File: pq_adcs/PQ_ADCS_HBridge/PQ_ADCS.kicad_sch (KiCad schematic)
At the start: 50 parts, among them J1 CES-110-02-L-S, J12 CES-102-02-L-S, J2 CES-110-02-L-S, J3 CES-110-02-L-S, J4 CES-110-02-L-S, J5 53261-1471, J6 53261-1471, J7 53261-1471, J8 53261-1471, U1 LPV542, U2 LPV542, U3 LPV542, U4 IIM-42652, U5 DRV8214RTER, U6 TMUX1108RSVR, U7 MMC5983MA, U8 DRV8214RTER, U9 DRV8214RTER

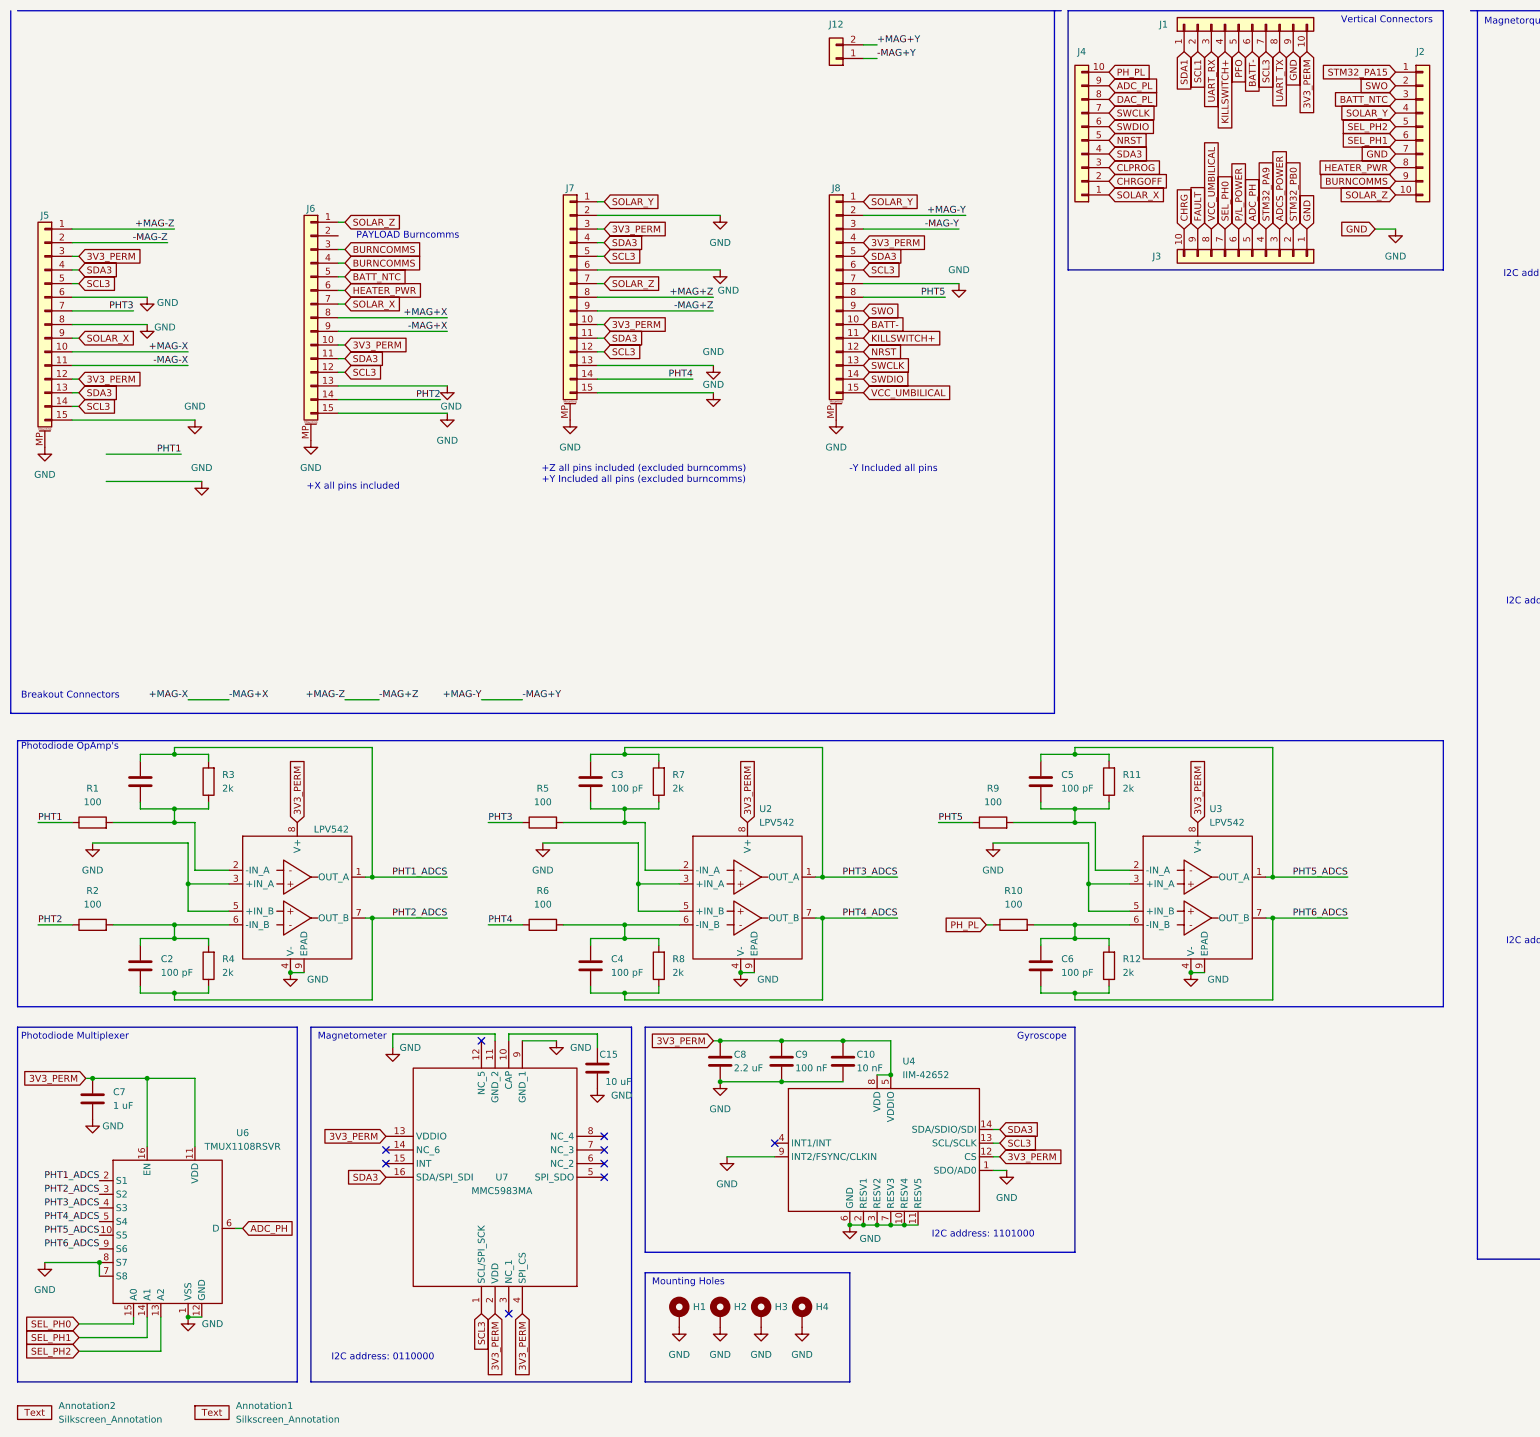
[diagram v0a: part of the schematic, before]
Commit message: ADCS_HBRIDGE backup restore
Restored version with H bridge and no connectors modification
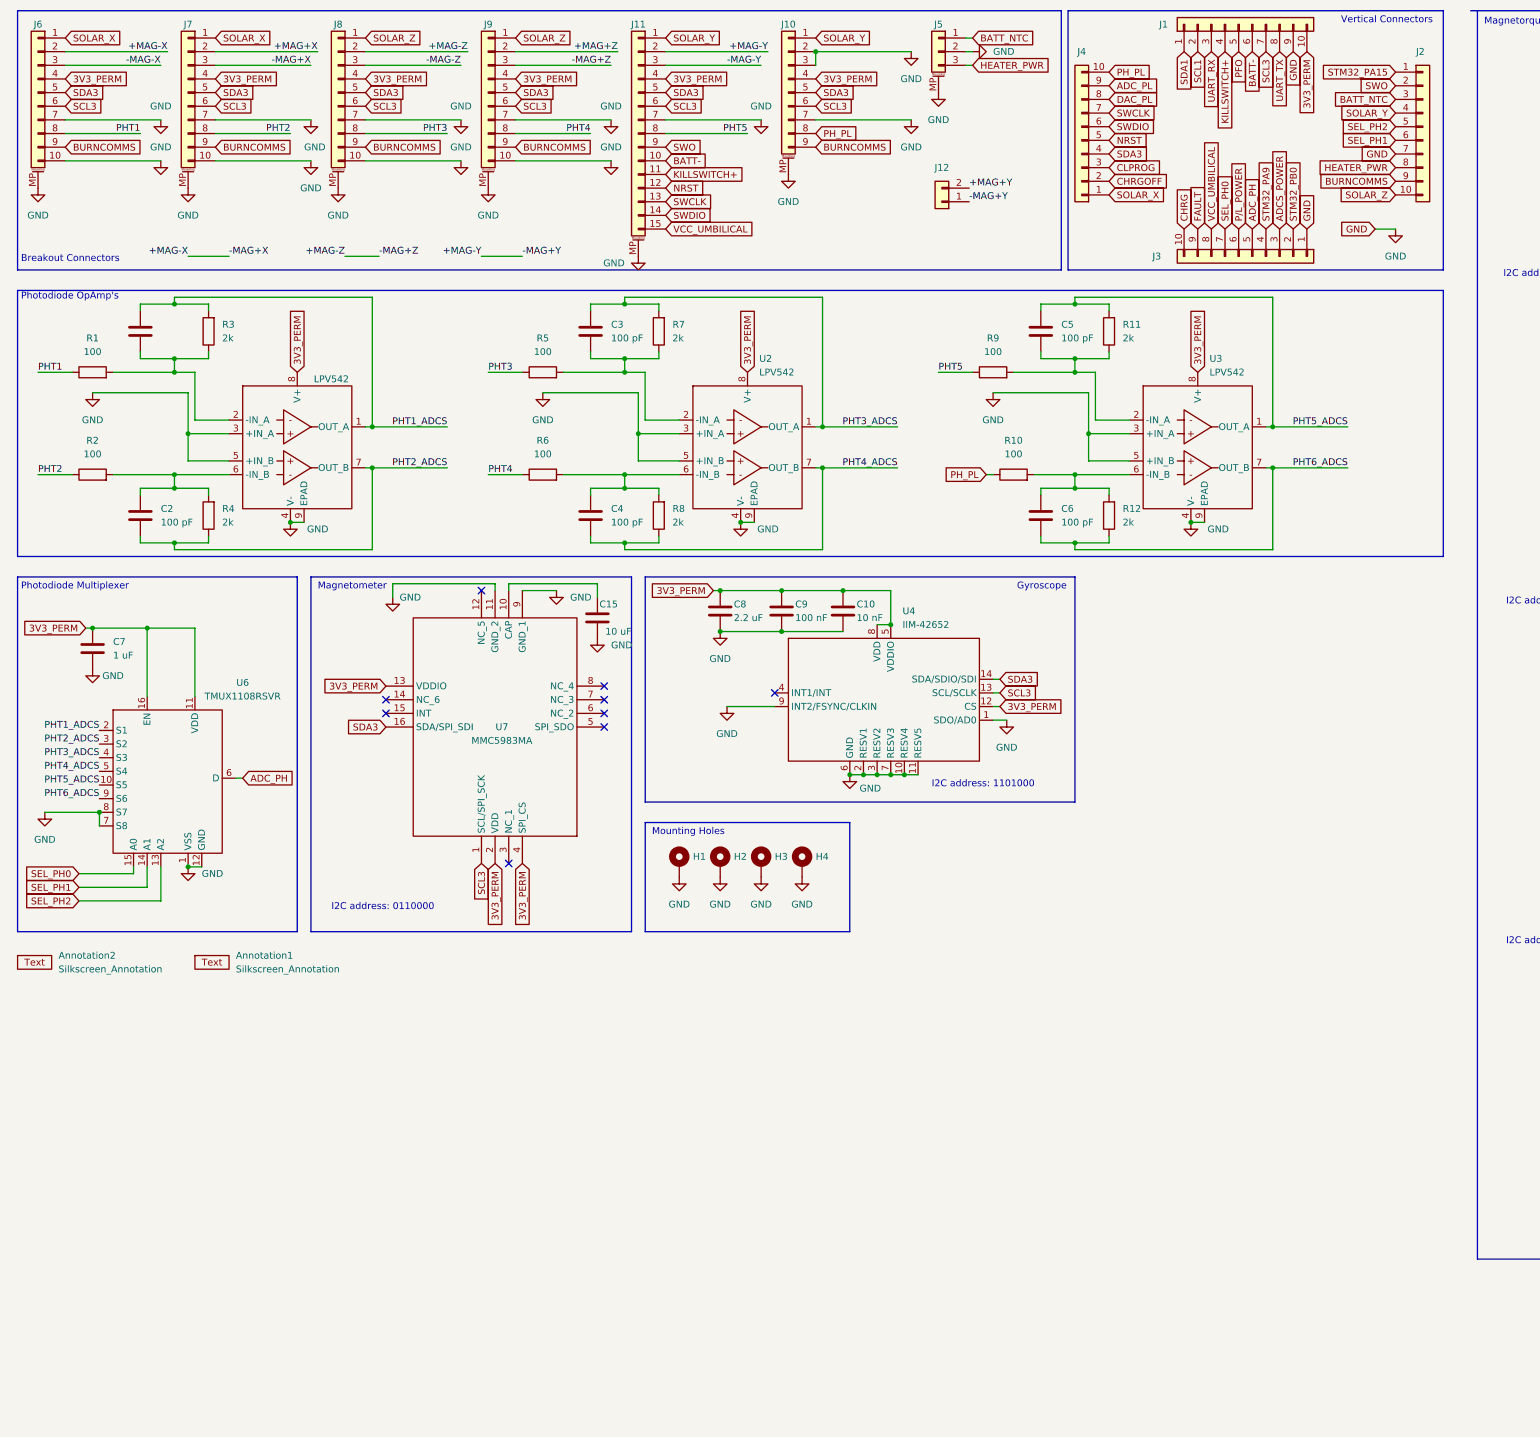
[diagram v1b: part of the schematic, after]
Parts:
- removed J5, J6, J7, J8: 53261-1471, Connector_Molex:Molex_PicoBlade_53261-1571_1x15-1MP_P1.25mm_Horizontal, symbol Connector_Generic_MountingPin:Conn_01x15_MountingPin
- added J10: Pico-Clasp_01x09, connector-nsl:Picoclasp09, symbol connector-nsl:Picoclasp09
- added J11: Pico-Clasp_01x15, connector-nsl:Picoclasp15, symbol connector-nsl:Picoclasp15
- added J5: Pico-Clasp_01x03, connector-nsl:Picoclasp03, symbol connector-nsl:Picoclasp03
- added J6, J7, J8, J9: Pico-Clasp_01x10, connector-nsl:Picoclasp10, symbol connector-nsl:Picoclasp10
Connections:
- net +MAG+X: now also J7.2
- net +MAG+Z: now also J9.2
- net +MAG-X: now also J6.2, J7.3
- net +MAG-Y: now also J11.2
- net +MAG-Z: now also J8.2, J9.3
- net -MAG-X: now also J6.3
- net -MAG-Y: now also J11.3
- net -MAG-Z: now also J8.3
- net 3V3_PERM: now also J10.4, J11.4, J6.4, J7.4, J8.4, J9.4
- net BATT-: now also J11.10
- net BATT_NTC: now also J5.1
- net BURNCOMMS: now also J10.9, J6.9, J7.9, J8.9, J9.9
- net GND: now also J10.2, J10.3, J10.7, J10.MP, J11.7, J11.MP, J5.2, J5.MP, J6.10, J6.7, J6.MP, J7.10, J7.7, J7.MP, J8.10, J8.7, J8.MP, J9.10, J9.7, J9.MP
- net HEATER_PWR: now also J5.3
- net KILLSWITCH+: now also J11.11
- net NRST: now also J11.12
- net PHT1: now also J6.8
- net PHT2: now also J7.8
- net PHT3: now also J8.8
- net PHT4: now also J9.8
- net PHT5: now also J11.8
- net PH_PL: now also J10.8
- net SCL3: now also J10.6, J11.6, J6.6, J7.6, J8.6, J9.6
- net SDA3: now also J10.5, J11.5, J6.5, J7.5, J8.5, J9.5
- net SOLAR_X: now also J6.1, J7.1
- net SOLAR_Y: now also J10.1, J11.1
- net SOLAR_Z: now also J8.1, J9.1
- net SWCLK: now also J11.13
- net SWDIO: now also J11.14
- net SWO: now also J11.9
- net VCC_UMBILICAL: now also J11.15
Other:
- note removed: "+X all pins included"
- note removed: "+Z all pins included (excluded burncomms) +Y Included all pins (excluded burncomms)"
- note removed: "-Y Included all pins"
- note removed: "PAYLOAD Burncomms"
- moved on the sheet: Annotation1, Annotation2, C10, C15, C2, C3, C4, C5, C6, C7, C8, C9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

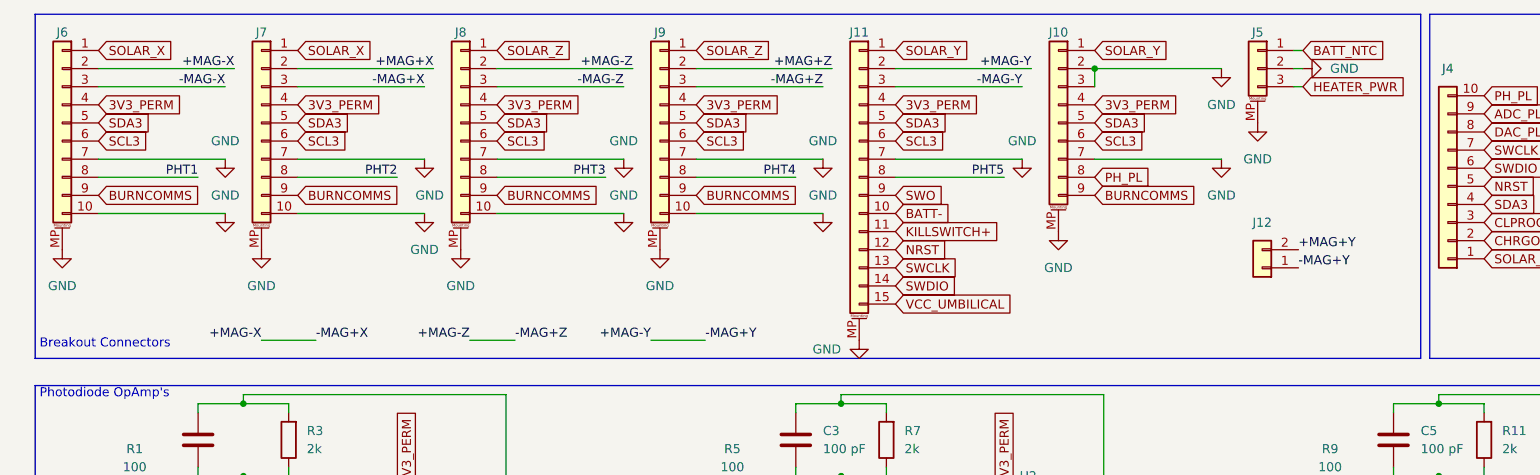
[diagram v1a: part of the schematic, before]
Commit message: MOdifying connectors ADCS H - Bridge
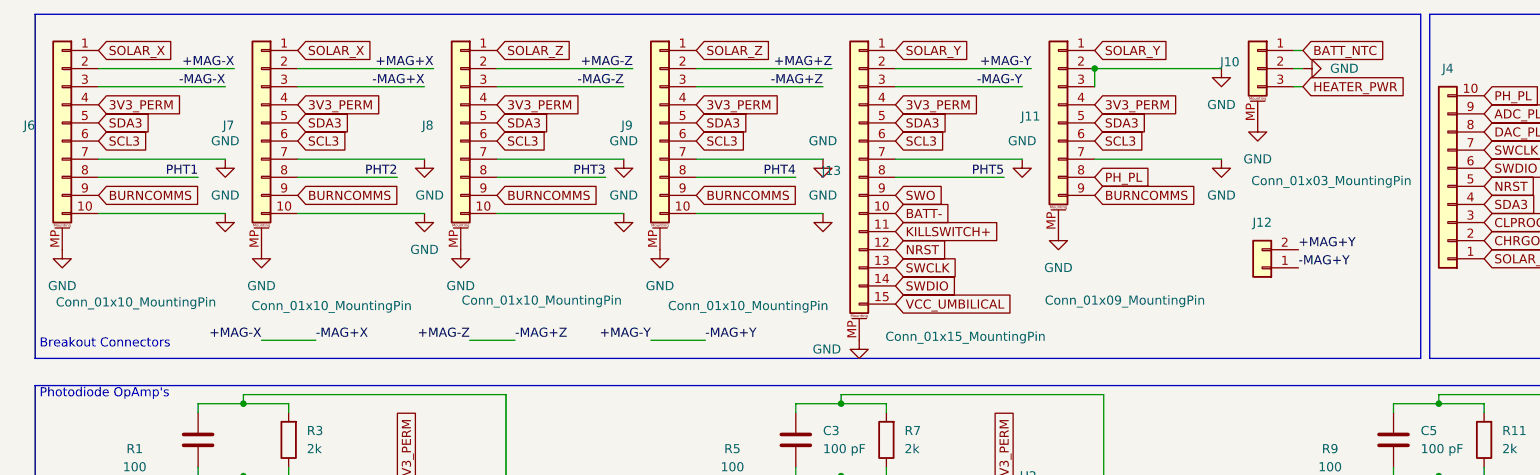
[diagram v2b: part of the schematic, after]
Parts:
- removed J10: Pico-Clasp_01x09, connector-nsl:Picoclasp09, symbol connector-nsl:Picoclasp09
- removed J11: Pico-Clasp_01x15, connector-nsl:Picoclasp15, symbol connector-nsl:Picoclasp15
- removed J5: Pico-Clasp_01x03, connector-nsl:Picoclasp03, symbol connector-nsl:Picoclasp03
- removed J6, J7, J8, J9: Pico-Clasp_01x10, connector-nsl:Picoclasp10, symbol connector-nsl:Picoclasp10
- added J10: Conn_01x03_MountingPin, Connector_Molex:Molex_PicoBlade_53261-0371_1x03-1MP_P1.25mm_Horizontal, symbol Connector_Generic_MountingPin:Conn_01x03_MountingPin
- added J11: Conn_01x09_MountingPin, Connector_Molex:Molex_PicoBlade_53261-0971_1x09-1MP_P1.25mm_Horizontal, symbol Connector_Generic_MountingPin:Conn_01x09_MountingPin
- added J13: Conn_01x15_MountingPin, Connector_Molex:Molex_PicoBlade_53261-1571_1x15-1MP_P1.25mm_Horizontal, symbol Connector_Generic_MountingPin:Conn_01x15_MountingPin
- added J6, J7, J8, J9: Conn_01x10_MountingPin, Connector_Molex:Molex_PicoBlade_53261-1071_1x10-1MP_P1.25mm_Horizontal, symbol Connector_Generic_MountingPin:Conn_01x10_MountingPin
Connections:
- net +MAG+X: now also J7.2 (Pin_2)
- net +MAG+Z: now also J9.2 (Pin_2)
- net +MAG-X: now also J6.2 (Pin_2), J7.3 (Pin_3)
- net +MAG-Y: now also J13.2 (Pin_2)
- net +MAG-Z: now also J8.2 (Pin_2), J9.3 (Pin_3)
- net -MAG-X: now also J6.3 (Pin_3)
- net -MAG-Y: now also J13.3 (Pin_3)
- net -MAG-Z: now also J8.3 (Pin_3)
- net 3V3_PERM: now also J11.4 (Pin_4), J13.4 (Pin_4), J6.4 (Pin_4), J7.4 (Pin_4), J8.4 (Pin_4), J9.4 (Pin_4)
- net BATT-: now also J13.10 (Pin_10)
- net BATT_NTC: now also J10.1 (Pin_1)
- net BURNCOMMS: now also J11.9 (Pin_9), J6.9 (Pin_9), J7.9 (Pin_9), J8.9 (Pin_9), J9.9 (Pin_9)
- net GND: now also J10.2 (Pin_2), J10.MP (MountPin), J11.2 (Pin_2), J11.3 (Pin_3), J11.7 (Pin_7), J11.MP (MountPin), J13.7 (Pin_7), J13.MP (MountPin), J6.10 (Pin_10), J6.7 (Pin_7), J6.MP (MountPin), J7.10 (Pin_10), J7.7 (Pin_7), J7.MP (MountPin), J8.10 (Pin_10), J8.7 (Pin_7), J8.MP (MountPin), J9.10 (Pin_10), J9.7 (Pin_7), J9.MP (MountPin)
- net HEATER_PWR: now also J10.3 (Pin_3)
- net KILLSWITCH+: now also J13.11 (Pin_11)
- net NRST: now also J13.12 (Pin_12)
- net PHT1: now also J6.8 (Pin_8)
- net PHT2: now also J7.8 (Pin_8)
- net PHT3: now also J8.8 (Pin_8)
- net PHT4: now also J9.8 (Pin_8)
- net PHT5: now also J13.8 (Pin_8)
- net PH_PL: now also J11.8 (Pin_8)
- net SCL3: now also J11.6 (Pin_6), J13.6 (Pin_6), J6.6 (Pin_6), J7.6 (Pin_6), J8.6 (Pin_6), J9.6 (Pin_6)
- net SDA3: now also J11.5 (Pin_5), J13.5 (Pin_5), J6.5 (Pin_5), J7.5 (Pin_5), J8.5 (Pin_5), J9.5 (Pin_5)
- net SOLAR_X: now also J6.1 (Pin_1), J7.1 (Pin_1)
- net SOLAR_Y: now also J11.1 (Pin_1), J13.1 (Pin_1)
- net SOLAR_Z: now also J8.1 (Pin_1), J9.1 (Pin_1)
- net SWCLK: now also J13.13 (Pin_13)
- net SWDIO: now also J13.14 (Pin_14)
- net SWO: now also J13.9 (Pin_9)
- net VCC_UMBILICAL: now also J13.15 (Pin_15)
